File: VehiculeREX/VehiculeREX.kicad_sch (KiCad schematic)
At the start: 0 parts

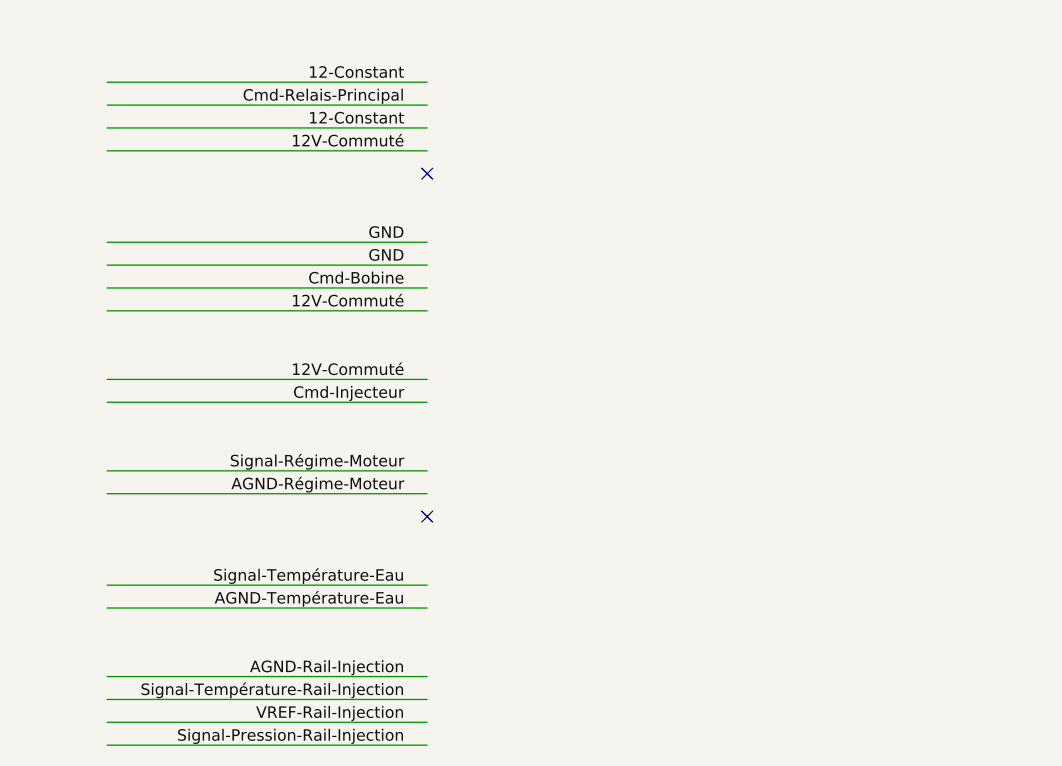
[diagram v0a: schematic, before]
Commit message: Corrections schema banc et début schéma véhicule
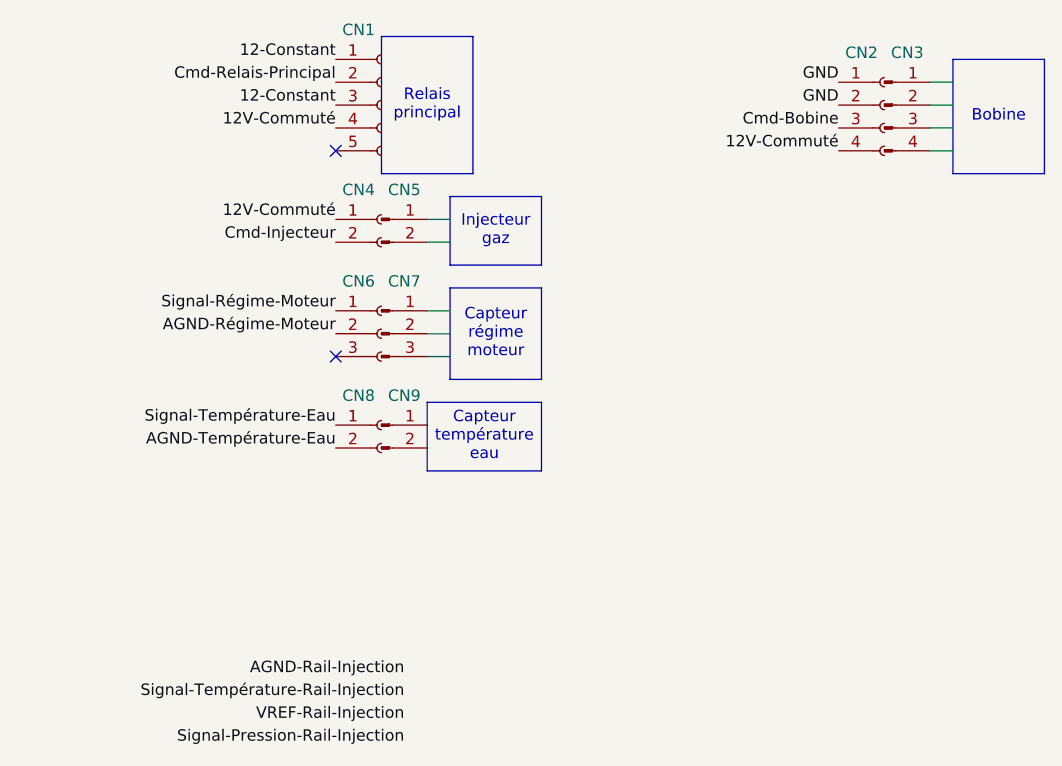
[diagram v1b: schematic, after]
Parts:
- added CN1: Relais principal, symbol Connector:Conn_01x05_Socket
- added CN2: Bobine, symbol Connector:Conn_01x04_Socket
- added CN3: Bobine, symbol Connector:Conn_01x04_Pin
- added CN4: Injecteur gaz, symbol Connector:Conn_01x02_Socket
- added CN5: Injecteur gaz, symbol Connector:Conn_01x02_Pin
- added CN6: Capteur régime moteur, symbol Connector:Conn_01x03_Socket
- added CN7: Capteur régime moteur, symbol Connector:Conn_01x03_Pin
- added CN8: Capteur température eau, symbol Connector:Conn_01x02_Socket
- added CN9: Capteur température eau, symbol Connector:Conn_01x02_Pin
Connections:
- net 12-Constant: now also CN1.1 (Pin_1), CN1.3 (Pin_3)
- net 12V-Commuté: now also CN1.4 (Pin_4), CN2.4 (Pin_4), CN4.1 (Pin_1)
- net AGND-Régime-Moteur: now also CN6.2 (Pin_2)
- net AGND-Température-Eau: now also CN8.2 (Pin_2)
- net Cmd-Bobine: now also CN2.3 (Pin_3)
- net Cmd-Injecteur: now also CN4.2 (Pin_2)
- net Cmd-Relais-Principal: now also CN1.2 (Pin_2)
- net GND: now also CN2.1 (Pin_1), CN2.2 (Pin_2)
- net Signal-Régime-Moteur: now also CN6.1 (Pin_1)
- net Signal-Température-Eau: now also CN8.1 (Pin_1)
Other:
- note added: "Bobine"
- note added: "Capteur régime moteur"
- note added: "Capteur température eau"
- note added: "Injecteur gaz"
- note added: "Relais principal"

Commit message: Corrections schema banc et continuation du schema véhicule
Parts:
- added CN10: Capteur Pression Température Rail Injection, symbol Connector:Conn_01x04_Socket
- added CN11: Capteur Pression Température Rail Injection, symbol Connector:Conn_01x04_Pin
- added CN12: Capteur Pression Température Air Admission, symbol Connector:Conn_01x04_Socket
- added CN13: Capteur Pression Température Air Admission, symbol Connector:Conn_01x04_Pin
- added CN14: Sonde Lambda UEGO, symbol Connector:Conn_01x06_Socket
- added CN15: Sonde Lambda UEGO, symbol Connector:Conn_01x06_Pin
- added CN16: Solenoide Bonbonne 1, symbol Connector:Conn_01x02_Socket
- added CN17: Solenoide Bonbonne 1, symbol Connector:Conn_01x02_Pin
- added CN18: Solenoide Bonbonne 2, symbol Connector:Conn_01x02_Socket
- added CN19: Solenoide Bonbonne 2, symbol Connector:Conn_01x02_Pin
- added CN20: Capteur Pression Détendeur, symbol Connector:Conn_01x03_Socket
- added CN21: Capteur Pression Détendeur, symbol Connector:Conn_01x03_Pin
- added CN22: Valve Détendeur, symbol Connector:Conn_01x02_Socket
- added CN23: Valve Détendeur, symbol Connector:Conn_01x02_Pin
- added CN24: Contact, symbol Connector:Conn_01x02_Pin
- added CN25: Contact, symbol Connector:Conn_01x02_Socket
- added CN26: Starting Function Changeover Switch Socket, symbol Connector:Conn_01x04_Socket
- added CN27: Starting Function Changeover Switch Socket, symbol Connector:Conn_01x04_Pin
- added CN28: Indicator Light Socket, symbol Connector:Conn_01x06_Socket
- added CN29: Indicator Light Socket, symbol Connector:Conn_01x06_Pin
- added CN30, CN33: Accelerator Control Stepper Motor Wires Socket, symbol Connector:Conn_01x05_Pin
- added CN31, CN32: Accelerator Control Stepper Motor Wires Socket, symbol Connector:Conn_01x05_Socket
- added CN34, CN36: Igniter Flameout Wire Socket, symbol Connector:Conn_01x02_Socket
- added CN35, CN37: Igniter Flameout Wire Socket, symbol Connector:Conn_01x02_Pin
- added CN38: Igniter Flameout Wire Socket, symbol Connector:Screw_Terminal_01x01
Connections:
- net 12-Constant: now also CN24.2 (Pin_2); no longer CN1.1 (Pin_1), CN1.3 (Pin_3)
- net 12V-Commuté: now also CN14.2 (Pin_2)
- net AGND-Rail-Injection: now also CN10.1 (Pin_1)
- net Signal-Pression-Rail-Injection: now also CN10.4 (Pin_4)
- net Signal-Température-Rail-Injection: now also CN10.2 (Pin_2)
- net VREF-Rail-Injection: now also CN10.3 (Pin_3)
- net GND renamed GND-Bobine
- net GND-Bobine: no longer CN2.1 (Pin_1)
- new net: CN35. (Pin_2), CN36.1 (Pin_1)
- new net: CN35. (Pin_2), CN36.2 (Pin_2)
- new net: CN31.1 (Pin_1), CN32.1 (Pin_1)
- new net: CN31.2 (Pin_2), CN32.2 (Pin_2)
- new net: CN31.3 (Pin_3), CN32.3 (Pin_3)
- new net: CN31.4 (Pin_4), CN32.4 (Pin_4)
- new net: CN31.5 (Pin_5), CN32.5 (Pin_5)
- new net 12V-Constant: CN1.1 (Pin_1), CN1.3 (Pin_3), CN34. (Pin_2)
- new net 5V-Papillon: CN30.5 (Pin_5)
- new net 5V-Pression-Détendeur: CN20.3 (Pin_3)
- new net AGND-Air-Admission: CN12.1 (Pin_1)
- new net Cmd-Bobine-1-Papillon: CN30.4 (Pin_4)
- new net Cmd-Bobine-2-Papillon: CN30.3 (Pin_3)
- new net Cmd-Bobine-3-Papillon: CN30.2 (Pin_2)
- new net Cmd-Bobine-4-Papillon: CN30.1 (Pin_1)
- new net Cmd-Contact: CN24.1 (Pin_1)
- new net Cmd-Driver-Bougie: CN34. (Pin_2)
- new net Cmd-Flameout-Engine: CN26.4 (Pin_4)
- new net Cmd-Solenoide-Bonbonne-1: CN16.1 (Pin_1)
- new net Cmd-Solenoide-Bonbonne-2: CN18.1 (Pin_1)
- new net Cmd-Start-Engine: CN26.2 (Pin_2)
- new net Cmd-Valve-Détendeur: CN22.1 (Pin_1)
- new net Common-Engine: CN26.3 (Pin_3)
- new net GND-Bonbonne-1: CN16.2 (Pin_2)
- new net GND-Bonbonne-2: CN18.2 (Pin_2)
- new net GND-Pression-Détendeur: CN20.1 (Pin_1)
- new net GND-Valve-Détendeur: CN22.2 (Pin_2)
- new net GND_Bobine: CN2.1 (Pin_1)
- new net Heater-Lambda: CN14.1 (Pin_1)
- new net IP-Lambda: CN14.3 (Pin_3)
- new net LED-Indicator-1: CN28.1 (Pin_1)
- new net LED-Indicator-2: CN28.2 (Pin_2)
- new net LED-Indicator-3: CN28.3 (Pin_3)
- new net RCOMP-Lambda: CN14.4 (Pin_4)
- new net Signal-Pression-Air-Admission: CN12.4 (Pin_4)
- new net Signal-Pression-Détendeur: CN20.2 (Pin_2)
- new net Signal-Température-Air-Admission: CN12.2 (Pin_2)
- new net VREF-Air-Admission: CN12.3 (Pin_3)
- new net VS-Lambda: CN14.5 (Pin_5)
- new net VSIP-Lambda: CN14.6 (Pin_6)
- no-connect marks 2 -> 7
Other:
- note added: "Accelerator Control Stepper Motor Wires Socket"
- note added: "Capteur Pression"
- note added: "Capteur pression température air admission"
- note added: "Capteur pression température rail injection"
- note added: "Détendeur"
- note added: "Engine Control Unit - Chinois"
- note added: "Igniter Flameout Wire Socket"
- note added: "Indicator Light Socket"
- note added: "Solenoide Bonbonne 1"
- note added: "Solenoide Bonbonne 2"
- note added: "Sonde lambda UEGO"
- note added: "Starting Function Changeover Switch Socket"
- note added: "Switch Contact"
- note added: "Valve"
- moved on the sheet: CN1, CN2, CN3, CN4, CN5, CN6, CN7, CN8, CN9

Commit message: Continuation
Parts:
- added CN39, CN40: Igniter Flameout Wire Socket, symbol Connector:Screw_Terminal_01x01
- added CN41: Generator Enable, symbol Connector:Conn_01x01_Socket
- added CN42: Generator Enable, symbol Connector:Conn_01x01_Pin
- added CN43, CN52: Phase 1, symbol Connector:Screw_Terminal_01x01
- added CN44, CN53: Phase 2, symbol Connector:Screw_Terminal_01x01
- added CN45, CN54: Phase 3, symbol Connector:Screw_Terminal_01x01
- added CN46: Switch Champignon Bonbonne 1, symbol Connector:Conn_01x02_Pin
- added CN47: Switch Champignon Bonbonne 1, symbol Connector:Conn_01x02_Socket
- added CN48, CN63: Switch Champignon Bonbonne 2, symbol Connector:Conn_01x02_Pin
- added CN49, CN64: Switch Champignon Bonbonne 2, symbol Connector:Conn_01x02_Socket
- added CN50: Switch Start/Flameout, symbol Connector:Conn_01x03_Socket
- added CN51: Switch Start/Flameout, symbol Connector:Conn_01x03_Pin
- added CN55: REX HV PDU, symbol Connector:Conn_01x04_Socket
- added CN56: REX HV PDU, symbol Connector:Conn_01x04_Male
- added CN57: Driver Bougie Chinois, symbol Connector:Conn_01x02_Pin
- added CN58: Driver Bougie Chinois, symbol Connector:Conn_01x02_Socket
- added CN59, CN60, CN61, CN62: Contacteur Haute-Tension, symbol Connector:Screw_Terminal_01x01
- added CN65, CN68: Switch Ventilateur, symbol Connector:Conn_01x02_Pin
- added CN66, CN67: Switch Ventilateur, symbol Connector:Conn_01x02_Socket
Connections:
- net 12-Constant is gone; now on net 12V-Constant: CN24.2 (Pin_2)
- net 12V-Constant: no longer CN34. (Pin_2)
- net 5V-Papillon: now also CN31.5 (Pin_5), CN32.5 (Pin_5)
- net Cmd-Bobine-1-Papillon: now also CN31.4 (Pin_4), CN32.4 (Pin_4)
- net Cmd-Bobine-2-Papillon: now also CN31.3 (Pin_3), CN32.3 (Pin_3)
- net Cmd-Bobine-3-Papillon: now also CN31.2 (Pin_2), CN32.2 (Pin_2)
- net Cmd-Bobine-4-Papillon: now also CN31.1 (Pin_1), CN32.1 (Pin_1)
- net Cmd-Driver-Bougie: now also CN35. (Pin_2), CN36.2 (Pin_2)
- net Cmd-Flameout-Engine: now also CN50.3 (Pin_3)
- net Cmd-Solenoide-Bonbonne-1: now also CN46.1 (Pin_1)
- net Cmd-Solenoide-Bonbonne-2: now also CN48.1 (Pin_1)
- net Cmd-Start-Engine: now also CN50.1 (Pin_1)
- net Common-Engine: now also CN50.2 (Pin_2)
- net 12V-Driver-Bougie: now reaches CN35. (Pin_2), CN36.1 (Pin_1)
- net 12V-Driver-Bougie: now also CN34. (Pin_2)
- net at CN15.1 (Pin_1): now also CN15.2 (Pin_2)
- net 12V-Commuté renamed 12V-Commuté-CRMT
- net GND-Bonbonne-1 renamed GND-Solenoide-Bonbonne-1
- net GND-Bonbonne-2 renamed GND-Solenoide-Bonbonne-2
- new net: CN55.A (Pin_A), CN55.B (Pin_B)
- new net 12V-Chauffe-Bougie: CN57.1 (Pin_1)
- new net 12V-Contacteur-HV: CN63.1 (Pin_1)
- new net 12V-ECU-FAN: CN65.1 (Pin_1)
- new net 12V-Engine-FAN: CN68.1 (Pin_1)
- new net 12V-Solenoide-Bonbonne-1: CN46.2 (Pin_2)
- new net 12V-Solenoide-Bonbonne-2: CN48.2 (Pin_2)
- new net Cmd-Contacteur-HV: CN61.1 (Pin_1), CN63.2 (Pin_2)
- new net Cmd-ECU-FAN: CN65.2 (Pin_2)
- new net Cmd-Engine-FAN: CN68.2 (Pin_2)
- new net Cmd-Generator: CN41.1 (Pin_1)
- new net GND-Chauffe-Bougie: CN57.2 (Pin_2)
- new net GND-Contacteur-HV: CN62.1 (Pin_1)
- new net REX-HV(+): CN39.1 (Pin_1), CN60.1 (Pin_1)
- new net REX-HV(+)-Commuté: CN55.1 (Pin_1), CN59.1 (Pin_1)
- new net REX-HV(-): CN40.1 (Pin_1), CN55.2 (Pin_2)
- new net REX-PHASE-1: CN43.1 (Pin_1), CN52.1 (Pin_1)
- new net REX-PHASE-2: CN44.1 (Pin_1), CN53.1 (Pin_1)
- new net REX-PHASE-3: CN45.1 (Pin_1), CN54.1 (Pin_1)
- no-connect marks 7 -> 8
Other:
- note added: "Bonbonne 1"
- note added: "Bonbonne 2"
- note added: "Bougie Chinoise"
- note added: "Contacteur HV"
- note added: "Driver Bougie Chinois"
- note added: "ECU"
- note added: "Generator Control"
- note added: "Generator Inputs"
- note added: "High Voltage Outputs"
- note added: "Moteur"
- note added: "Moteur Papillon"
- note added: "Power Distribution Unit"
- note added: "REX Engine"
- note added: "Switch Champignon Bonbonne"
- note added: "Switch Champignon Contacteur HV"
- note added: "Switch Generator Enable"
- note added: "Switch Start/Flameout"
- note added: "Switch Valve Détendeur"
- note added: "Switch Ventilateur"
- note added: "Switch à clef Contact"
- note added: "Ventilateur ECU"
- note added: "Ventilateur Moteur"
- note removed: "Switch Contact"
- moved on the sheet: CN28, CN29, CN30, CN31, CN32, CN33, CN34, CN35, CN36, CN37, CN38

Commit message: Le cauchemar continue
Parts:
- removed CN30: Accelerator Control Stepper Motor Wires Socket, symbol Connector:Conn_01x05_Pin
- removed CN31: Accelerator Control Stepper Motor Wires Socket, symbol Connector:Conn_01x05_Socket
- added CN1: ECU - CRMT, symbol Connector:Conn_01x02_Socket
- added CN2: ECU - CRMT, symbol Connector:Conn_01x02_Pin
- added CN28: Capteur température eau, symbol Connector:Conn_01x02_Socket
- added CN29: Capteur Température Echappement, symbol Connector:Conn_01x02_Pin
- added CN3: ECU - CRMT, symbol Connector:Conn_01x17_Pin
- added CN4: ECU - CRMT, symbol Connector:Conn_01x17_Socket
- added CN5: ECU - CRMT, symbol Connector:Conn_01x14_Socket
- added CN57: Papillon, symbol Connector:Conn_01x06_Socket
- added CN58: Papillon, symbol Connector:Conn_01x06_Pin
- added CN6: ECU - CRMT, symbol Connector:Conn_01x14_Pin
- added CN63: CAN 1, symbol Connector:Conn_01x02_Socket
- added CN64: CAN 2, symbol Connector:Conn_01x02_Socket
- added CN77: Switch Valve Détendeur, symbol Connector:Conn_01x02_Pin
- added CN78: Switch Valve Détendeur, symbol Connector:Conn_01x02_Socket
- added CN79: Switch Generator Enable, symbol Connector:Conn_01x02_Socket
- added CN80: Switch Generator Enable, symbol Connector:Conn_01x02_Pin
- added F1: 100A, symbol Device:Fuse
- CN10: renamed from CN28; value Indicator Light Socket -> ECU Chinois
- CN11: renamed from CN32; value Accelerator Control Stepper Motor Wires Socket -> ECU Chinois
- CN12: renamed from CN33; value Accelerator Control Stepper Motor Wires Socket -> ECU Chinois
- CN13: renamed from CN35; value Igniter Flameout Wire Socket -> ECU Chinois
- CN14: renamed from CN34; value Igniter Flameout Wire Socket -> ECU Chinois
- CN15: renamed from CN37; value Igniter Flameout Wire Socket -> ECU Chinois
- CN16: renamed from CN36; value Igniter Flameout Wire Socket -> ECU Chinois
- CN17: renamed from CN38; value Igniter Flameout Wire Socket -> ECU Chinois
- CN18: renamed from CN39; value Igniter Flameout Wire Socket -> ECU Chinois
- CN19: renamed from CN40; value Igniter Flameout Wire Socket -> ECU Chinois
- CN20: renamed from CN41; value Generator Enable -> ECU Chinois
- CN21: renamed from CN42; value Generator Enable -> ECU Chinois
- CN22: renamed from CN43; value Phase 1 -> ECU Chinois
- CN23: renamed from CN44; value Phase 2 -> ECU Chinois
- CN24: renamed from CN45; value Phase 3 -> ECU Chinois
- CN7: renamed from CN27; value Starting Function Changeover Switch Socket -> ECU Chinois
- CN8: renamed from CN26; value Starting Function Changeover Switch Socket -> ECU Chinois
- CN9: renamed from CN29; value Indicator Light Socket -> ECU Chinois
- renumbered CN1 to CN25, CN7 to CN26, CN6 to CN27, CN8 to CN30, CN9 to CN31, CN11 to CN32, CN10 to CN33, CN12 to CN34, CN13 to CN35, CN14 to CN36, CN15 to CN37, CN20 to CN38, CN21 to CN39, CN22 to CN40, CN23 to CN41, CN17 to CN42, CN16 to CN43, CN19 to CN44, CN18 to CN45, CN3 to CN46, CN2 to CN47, CN4 to CN48, CN5 to CN49, CN52 to CN50, CN53 to CN51, CN54 to CN52, CN59 to CN53, CN60 to CN54, CN61 to CN55, CN62 to CN56, CN55 to CN59, CN56 to CN60, CN57 to CN61, CN58 to CN62, CN24 to CN65, CN25 to CN66, CN46 to CN67, CN47 to CN68, CN48 to CN69, CN49 to CN70, CN51 to CN71, CN50 to CN72, CN65 to CN73, CN66 to CN74, CN67 to CN75, CN68 to CN76, CN63 to CN81, CN64 to CN82
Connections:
- net 12V-Commuté-CRMT: now also CN5.M1 (Pin_11), CN5.M2 (Pin_12), CN5.M3 (Pin_13), CN5.M4 (Pin_14)
- net 12V-Valve-Détendeur: now also CN77.1 (Pin_1)
- net AGND-Air-Admission: now also CN4.D4 (Pin_D4)
- net AGND-Rail-Injection: now also CN4.F4 (Pin_F4)
- net AGND-Régime-Moteur: now also CN4.J4 (Pin_J4)
- net AGND-Température-Eau: now also CN4.G4 (Pin_G4)
- net Cmd-Bobine: now also CN1.F3 (Pin_F3)
- net Cmd-Contact: now also CN5.C4 (Pin_1)
- net Cmd-Generator: now also CN80.2 (Pin_2)
- net Cmd-Injecteur: now also CN1.E4 (Pin_E4)
- net Cmd-Relais-Principal: now also CN5.H2 (Pin_2)
- net Cmd-Valve-Détendeur: now also CN77.2 (Pin_2)
- net Heater-Lambda: now also CN4.M4 (Pin_M4)
- net IP-Lambda: now also CN4.K2 (Pin_K2)
- net RCOMP-Lambda: now also CN4.J1 (Pin_J1)
- net REX-HV(+): now also CN80.1 (Pin_1)
- net Signal-Pression-Air-Admission: now also CN4.D2 (Pin_D2)
- net Signal-Pression-Rail-Injection: now also CN4.B1 (Pin_B1)
- net Signal-Régime-Moteur: now also CN4.A1 (Pin_A1)
- net Signal-Température-Air-Admission: now also CN4.E2 (Pin_E2)
- net Signal-Température-Eau: now also CN4.F1 (Pin_F1)
- net Signal-Température-Rail-Injection: now also CN4.E1 (Pin_E1)
- net VREF-Air-Admission: now also CN4.L3 (Pin_L3)
- net VREF-Rail-Injection: now also CN4.K4 (Pin_K4)
- net VS-Lambda: now also CN4.K1 (Pin_K1)
- net VSIP-Lambda: now also CN4.J2 (Pin_J2)
- net 5V-Papillon: no longer names the net of CN11.5 (Pin_5)
- net Cmd-Bobine-1-Papillon: no longer names the net of CN11.4 (Pin_4)
- net Cmd-Bobine-2-Papillon: no longer names the net of CN11.3 (Pin_3)
- net Cmd-Bobine-3-Papillon: no longer names the net of CN11.2 (Pin_2)
- net Cmd-Bobine-4-Papillon: no longer names the net of CN11.1 (Pin_1)
- new net AGND-Température-Echappement: CN28.2 (Pin_2), CN4.F3 (Pin_F3)
- new net CAN1-H: CN5.J2 (Pin_4), CN63.7 (Pin_7)
- new net CAN1-L: CN5.J1 (Pin_3), CN63.2 (Pin_2)
- new net CAN2-H: CN5.J4 (Pin_6), CN64.7 (Pin_7)
- new net CAN2-L: CN5.J3 (Pin_5), CN64.2 (Pin_2)
- new net Capteur(+)-Papillon: CN4.L1 (Pin_L1), CN57.3 (Pin_3)
- new net Capteur(-)-Papillon: CN4.G3 (Pin_G3), CN57.2 (Pin_2)
- new net GND-CRMT: CN5.L1 (Pin_7), CN5.L2 (Pin_8), CN5.L3 (Pin_9), CN5.L4 (Pin_10)
- new net Moteur(+)-Papillon: CN4.M2 (Pin_M2), CN57.4 (Pin_4)
- new net Moteur(-)-Papillon: CN4.M1 (Pin_M1), CN57.1 (Pin_1)
- new net Signal-Position-1-Papillon: CN4.A3 (Pin_A3), CN57.6 (Pin_6)
- new net Signal-Position-2-Papillon: CN4.A4 (Pin_A4), CN57.5 (Pin_5)
- new net Signal-Température-Echappement: CN28.1 (Pin_1), CN4.F2 (Pin_F2)
- no-connect marks 8 -> 13
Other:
- note added: "CAN 1"
- note added: "CAN 2"
- note added: "Capteur température echappement"
- note added: "Engine Control Unit - CRMT"
- note added: "Papillon"
- note removed: "Moteur Papillon"
- moved on the sheet: CN10, CN11, CN12, CN13, CN14, CN15, CN16, CN17, CN18, CN19, CN20, CN21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

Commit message: Bis repetita
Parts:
- removed CN25: Relais principal, symbol Connector:Conn_01x05_Socket
- removed CN53, CN54, CN55, CN56: Contacteur Haute-Tension, symbol Connector:Screw_Terminal_01x01
- removed CN61: Driver Bougie Chinois, symbol Connector:Conn_01x02_Pin
- removed CN62: Driver Bougie Chinois, symbol Connector:Conn_01x02_Socket
- removed CN65: Contact, symbol Connector:Conn_01x02_Pin
- removed CN66: Contact, symbol Connector:Conn_01x02_Socket
- removed CN67: Switch Champignon Bonbonne 1, symbol Connector:Conn_01x02_Pin
- removed CN68: Switch Champignon Bonbonne 1, symbol Connector:Conn_01x02_Socket
- removed CN69, CN81: Switch Champignon Bonbonne 2, symbol Connector:Conn_01x02_Pin
- removed CN70, CN82: Switch Champignon Bonbonne 2, symbol Connector:Conn_01x02_Socket
- removed CN71: Switch Start/Flameout, symbol Connector:Conn_01x03_Pin
- removed CN72: Switch Start/Flameout, symbol Connector:Conn_01x03_Socket
- removed CN73: Switch Ventilateur, symbol Connector:Conn_01x02_Pin
- removed CN74: Switch Ventilateur, symbol Connector:Conn_01x02_Socket
- removed CN77: Switch Valve Détendeur, symbol Connector:Conn_01x02_Pin
- removed CN78: Switch Valve Détendeur, symbol Connector:Conn_01x02_Socket
- removed CN79: Switch Generator Enable, symbol Connector:Conn_01x02_Socket
- removed CN80: Switch Generator Enable, symbol Connector:Conn_01x02_Pin
- added K1: BT-REX, symbol Relay:Relay_SPDT
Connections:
- net Cmd-Solenoide-Bonbonne-1 is gone; now on net Cmd-Contact: CN43.1 (Pin_1)
- net Cmd-Solenoide-Bonbonne-2 is gone; now on net Cmd-Contact: CN45.1 (Pin_1)
- net Cmd-Valve-Détendeur is gone; now on net Cmd-Contact: CN40.1 (Pin_1)
- net REX-HV(+)-Commuté is gone; now on net REX-HV(+): CN59.1 (Pin_1)
- net Cmd-Contact: now also K1.88
- new net 12V-DCDC: K1.30, K1.85
- new net Cmd-Relai-BT: K1.86
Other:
- note added: "CRMT"
- note removed: "Bonbonne 1"
- note removed: "Bonbonne 2"
- note removed: "Bougie Chinoise"
- note removed: "Contacteur HV"
- note removed: "ECU"
- note removed: "Moteur"
- note removed: "Relais principal"
- note removed: "Switch Champignon Bonbonne"
- note removed: "Switch Champignon Contacteur HV"
- note removed: "Switch Generator Enable"
- note removed: "Switch Start/Flameout"
- note removed: "Switch Valve Détendeur"
- note removed: "Switch Ventilateur"
- note removed: "Switch à clef Contact"
- moved on the sheet: CN50, CN51, CN52, CN59, CN60, CN63, CN64, CN75, CN76
